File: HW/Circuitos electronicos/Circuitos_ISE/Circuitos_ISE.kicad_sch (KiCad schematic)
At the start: 36 parts, among them J1 Conn_01x02, U1 TL074, U2 LM2596S-ADJ, U2 TL074

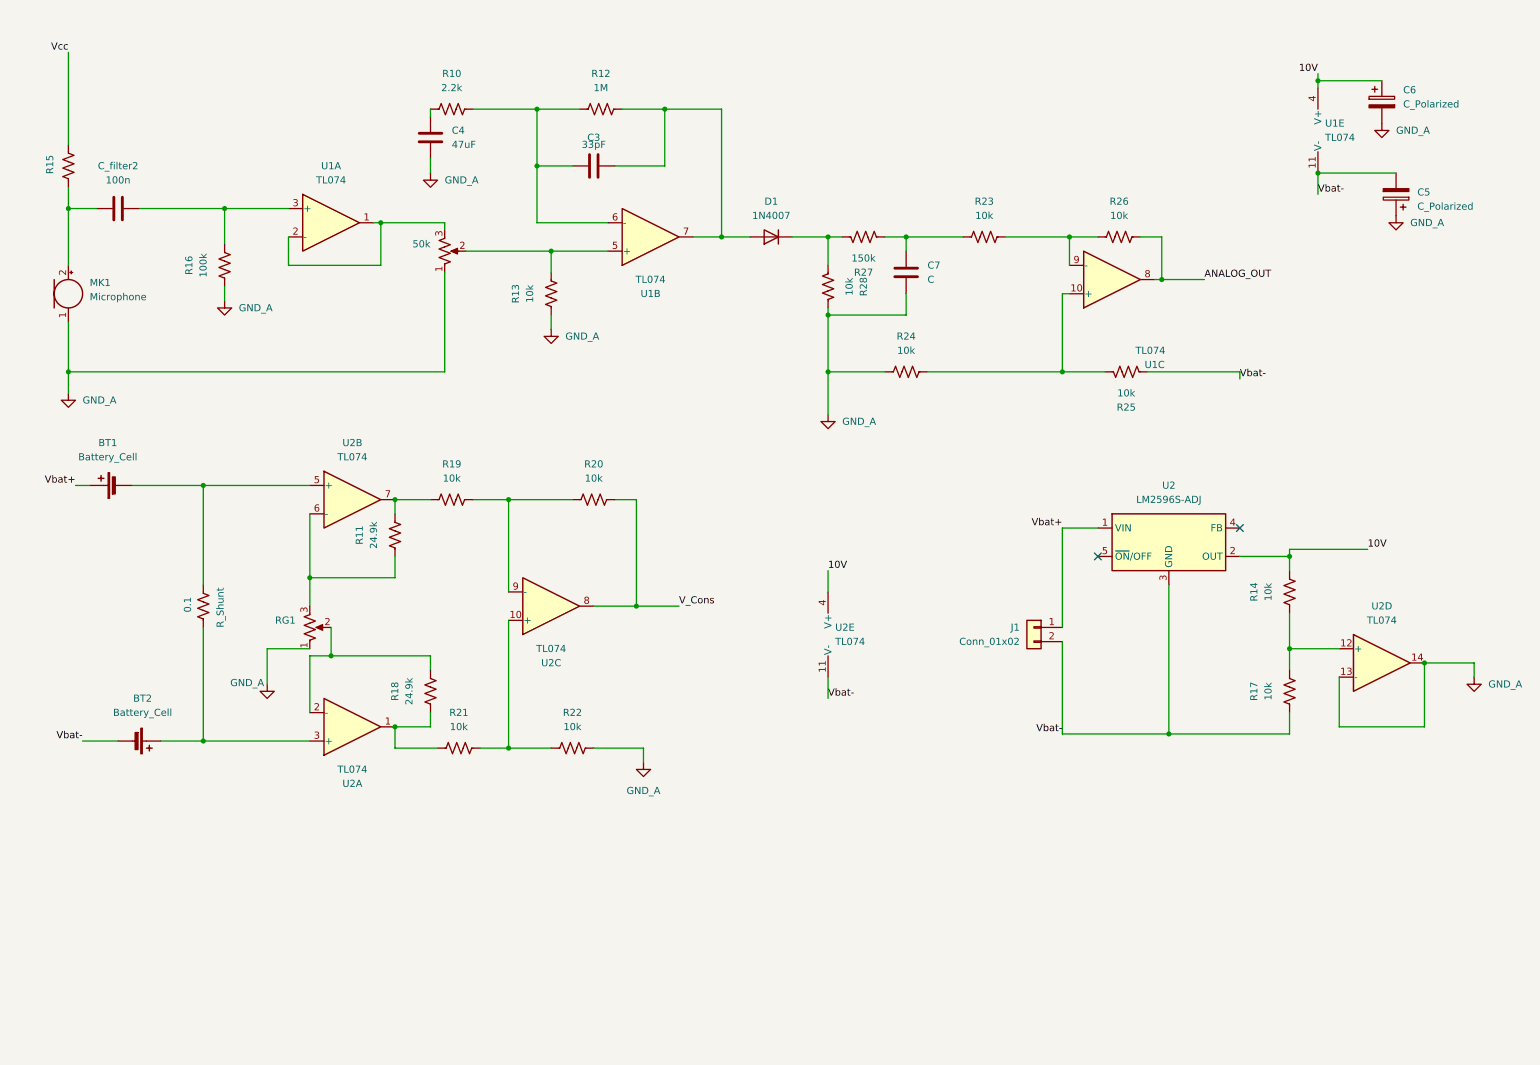
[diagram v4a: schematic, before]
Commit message: Actualizacion de el circuito analogico y codigo del ADC
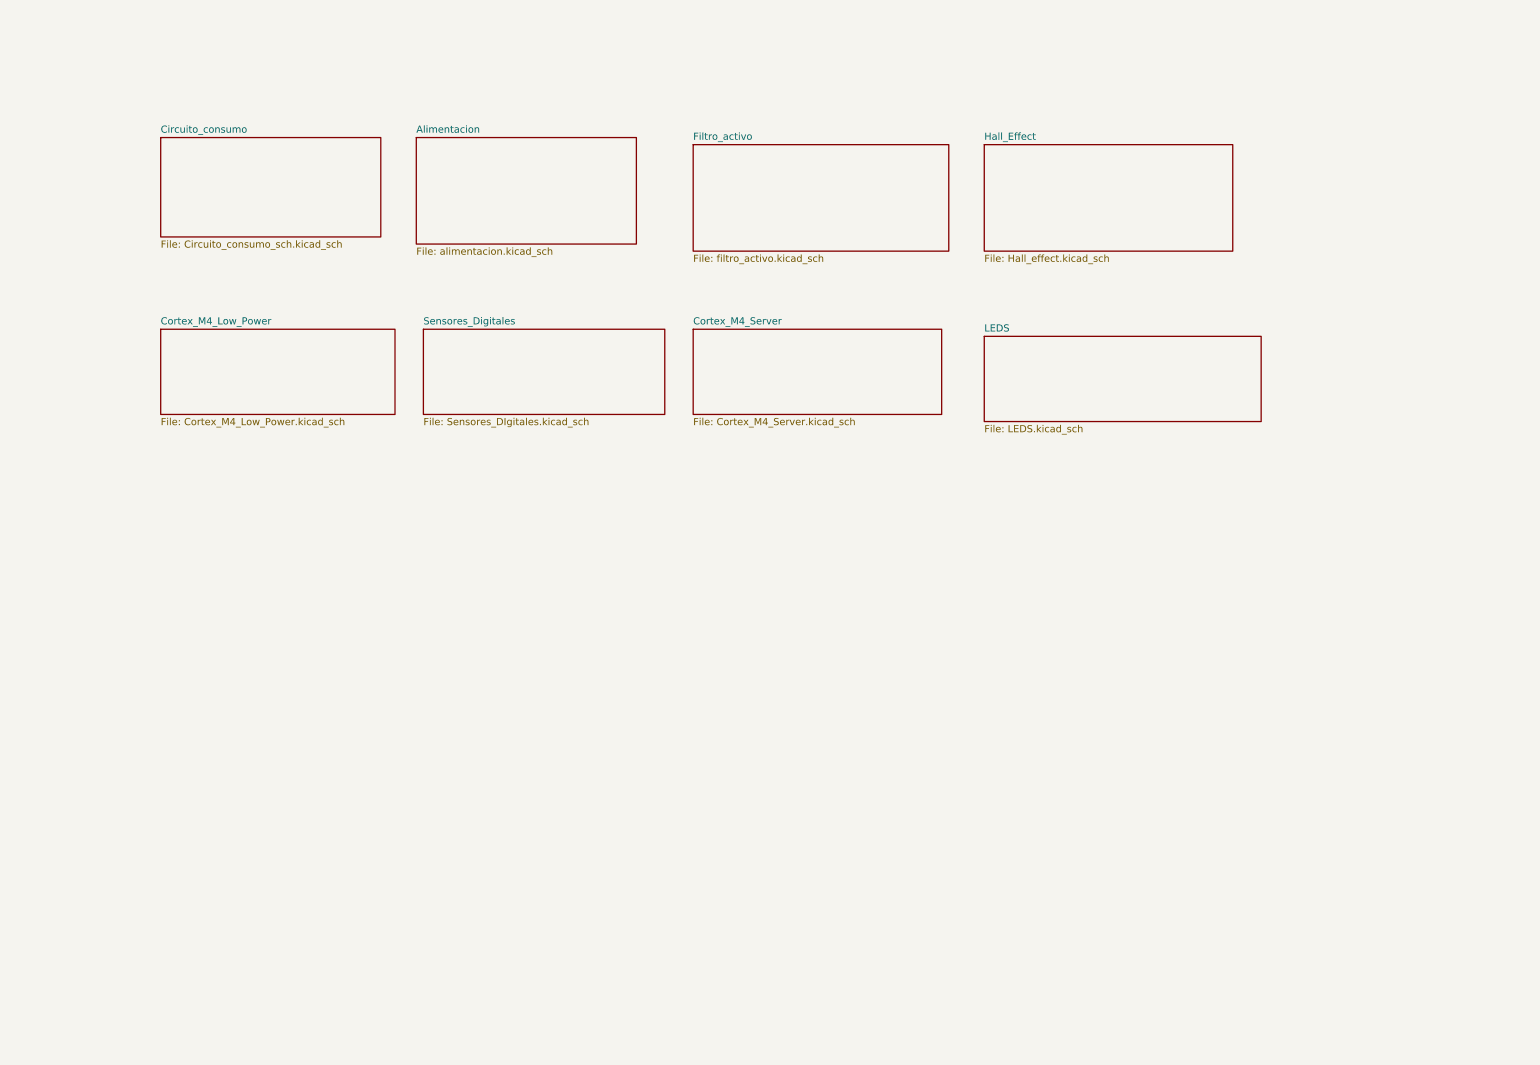
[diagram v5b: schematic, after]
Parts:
- removed 50k, RG1: R_Potentiometer_US, symbol Device:R_Potentiometer_US
- removed BT1, BT2: Battery_Cell, symbol Device:Battery_Cell
- removed C3: 33pF, symbol Device:C
- removed C4: 47uF, symbol Device:C
- removed C5, C6: C_Polarized, symbol Device:C_Polarized
- removed C7: C, symbol Device:C
- removed C_filter2: 100n, symbol Device:C
- removed D1: 1N4007, Diode_THT:D_DO-41_SOD81_P10.16mm_Horizontal, symbol Diode:1N4007
- removed J1: Conn_01x02, symbol Connector_Generic:Conn_01x02
- removed MK1: Microphone, symbol Device:Microphone
- removed R10: 2.2k, symbol Device:R_US
- removed R11, R18: 24.9k, symbol Device:R_US
- removed R12: 1M, symbol Device:R_US
- removed R13, R14, R17, R19, R20, R21, R22, R23, R24, R25, R26, R28: 10k, symbol Device:R_US
- removed R15: R_US, symbol Device:R_US
- removed R16: 100k, symbol Device:R_US
- removed R27: 150k, symbol Device:R_US
- removed R_Shunt: 0.1, symbol Device:R_US
- removed U1, U2: TL074, symbol Amplifier_Operational:TL074
- removed U2: LM2596S-ADJ, Package_TO_SOT_SMD:TO-263-5_TabPin3, symbol Regulator_Switching:LM2596S-ADJ
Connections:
- no-connect marks 2 -> 0
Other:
- added sheet Alimentacion (alimentacion.kicad_sch)
- added sheet Circuito_consumo (Circuito_consumo_sch.kicad_sch)
- added sheet Cortex_M4_Low_Power (Cortex_M4_Low_Power.kicad_sch)
- added sheet Cortex_M4_Server (Cortex_M4_Server.kicad_sch)
- added sheet Filtro_activo (filtro_activo.kicad_sch)
- added sheet Hall_Effect (Hall_effect.kicad_sch)
- added sheet LEDS (LEDS.kicad_sch)
- added sheet Sensores_Digitales (Sensores_DIgitales.kicad_sch)
